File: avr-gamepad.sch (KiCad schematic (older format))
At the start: 31 parts, among them J1 Conn_01x08, P1 USB_C_Plug_USB2.0, SW1 RESET, SW10 Up, SW11 Down, SW12 Left, SW13 Select, SW2 R, SW3 X, SW4 A, SW5 B, SW6 Start, SW7 Y, SW8 Right, SW9 L, U1 ATmega32U4-AU, Y1 16 MHz

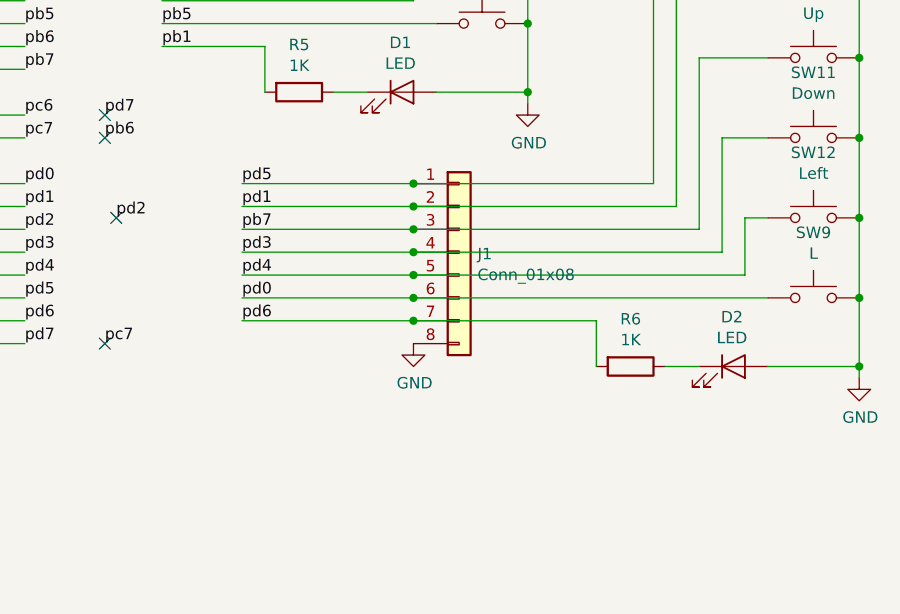
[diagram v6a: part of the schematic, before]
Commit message: kill the double sided feature, make it 2 boards, import mousebites
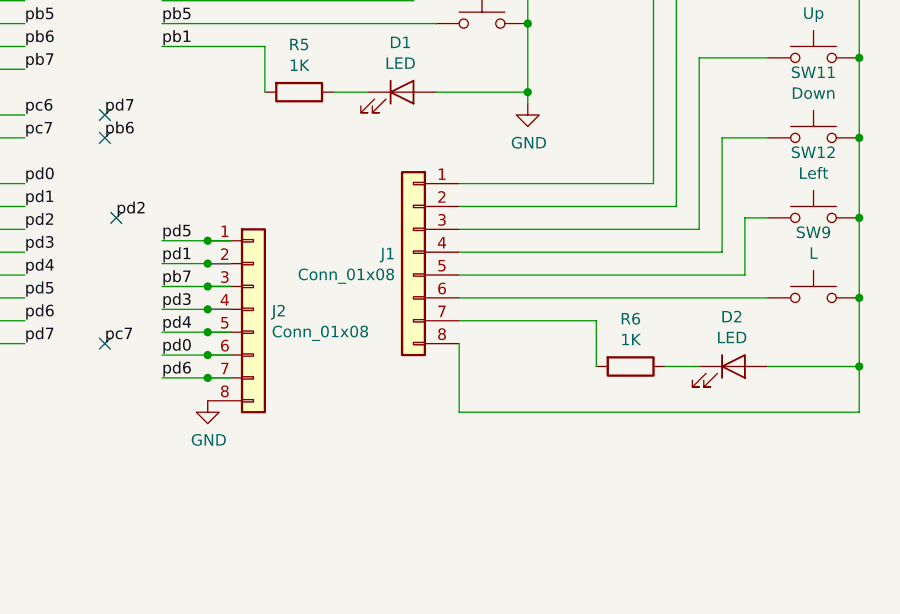
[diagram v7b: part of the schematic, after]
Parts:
- added J2: Conn_01x08, Connector_FFC-FPC:Hirose_FH12-8S-0.5SH_1x08-1MP_P0.50mm_Horizontal, symbol Connector_Generic:Conn_01x08
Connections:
- wire segments 135 -> 144
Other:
- moved on the sheet: J1
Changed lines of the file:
@@
 	6600 850  7100 850
 Connection ~ 8950 3800
-$Comp
-L power:GND #PWR0115
-U 1 1 5CF1335E
-P 8950 4150
-F 0 "#PWR0115" H 8950 3900 50  0001 C CNN
-F 1 "GND" H 8955 3977 50  0000 C CNN
-F 2 "" H 8950 4150 50  0001 C CNN
-F 3 "" H 8950 4150 50  0001 C CNN
-	1    8950 4150
-	1    0    0    -1
-$EndComp
 Wire Wire Line
 	8950 3450 8950 3800
@@
 	8550 4100 8950 4100
 Connection ~ 8950 4100
-Wire Wire Line
-	8950 4100 8950 4150
 Wire Wire Line
 	7800 4100 7800 3900
@@
 	1400 4400 1400 4550
 Wire Wire Line
-	6250 3900 7000 3900
-Wire Wire Line
-	6250 3800 7000 3800
-Wire Wire Line
-	6250 3700 7000 3700
-Wire Wire Line
-	6250 3600 7000 3600
-Wire Wire Line
-	6250 3500 7000 3500
-Wire Wire Line
-	6250 3400 7000 3400
-Wire Wire Line
-	6250 3300 7000 3300
-Connection ~ 7000 3300
-Wire Wire Line
-	7000 3300 8050 3300
-Connection ~ 7000 3400
-Wire Wire Line
-	7000 3400 8150 3400
-Connection ~ 7000 3500
-Wire Wire Line
-	7000 3500 8250 3500
-Connection ~ 7000 3600
-Wire Wire Line
-	7000 3600 8350 3600
-Connection ~ 7000 3700
-Wire Wire Line
-	7000 3700 8450 3700
-Connection ~ 7000 3800
-Wire Wire Line
-	7000 3800 8550 3800
-Connection ~ 7000 3900
-Wire Wire Line
-	7000 3900 7800 3900
+	5900 4150 6100 4150
+Wire Wire Line
+	5900 4050 6100 4050
+Wire Wire Line
+	5900 3950 6100 3950
+Wire Wire Line
+	5900 3850 6100 3850
+Wire Wire Line
+	5900 3750 6100 3750
+Wire Wire Line
+	5900 3650 6100 3650
+Wire Wire Line
+	5900 3550 6100 3550
 Text Label 5300 2800 0    50   ~ 0
 pb7
@@
 Text Label 5900 2600 0    50   ~ 0
 pb5
-Text Label 6250 3400 0    50   ~ 0
+Text Label 5900 3650 0    50   ~ 0
 pd1
 Text Label 5700 3450 0    50   ~ 0
 pd2
-Text Label 6250 3600 0    50   ~ 0
+Text Label 5900 3850 0    50   ~ 0
 pd3
-Text Label 6250 3700 0    50   ~ 0
+Text Label 5900 3950 0    50   ~ 0
 pd4
-Text Label 6250 3300 0    50   ~ 0
+Text Label 5900 3550 0    50   ~ 0
 pd5
 Text Label 5650 3000 0    50   ~ 0
@@
 	5100 3900 5300 3900
 NoConn ~ 5700 3450
-Text Label 6250 3500 0    50   ~ 0
+Text Label 5900 3750 0    50   ~ 0
 pb7
 NoConn ~ 5100 4300
@@
 	1    0    0    -1
 $EndComp
-Text Label 6250 3900 0    50   ~ 0
+Text Label 5900 4150 0    50   ~ 0
 pd6
 NoConn ~ 5650 3000
 NoConn ~ 5650 4000
-$Comp
-L power:GND #PWR0113
-U 1 1 5D261ED2
-P 7000 4000
-F 0 "#PWR0113" H 7000 3750 50  0001 C CNN
-F 1 "GND" H 7005 3827 50  0000 C CNN
-F 2 "" H 7000 4000 50  0001 C CNN
-F 3 "" H 7000 4000 50  0001 C CNN
-	1    7000 4000
-	1    0    0    -1
-$EndComp
-$Comp
-L Connector_Generic:Conn_01x08 J1
-U 1 1 5CF089CD
-P 7200 3600
-F 0 "J1" H 7280 3592 50  0000 L CNN
-F 1 "Conn_01x08" H 7280 3501 50  0000 L CNN
-F 2 "Connector_FFC-FPC:Hirose_FH12-8S-0.5SH_1x08-1MP_P0.50mm_Horizontal" H 7200 3600 50  0001 C CNN
-F 3 "~" H 7200 3600 50  0001 C CNN
-	1    7200 3600
-	1    0    0    -1
-$EndComp
 Text Label 5650 4000 0    50   ~ 0
 pc7
@@
 Text Label 5900 2100 0    50   ~ 0
 pb3
-Text Label 6250 3800 0    50   ~ 0
+Text Label 5900 4050 0    50   ~ 0
 pd0
 $Comp
@@
 Wire Wire Line
 	1150 1850 2350 1850
+$Comp
+L Connector_Generic:Conn_01x08 J2
+U 1 1 5D94373B
+P 6300 3850
+F 0 "J2" H 6380 3842 50  0000 L CNN
+F 1 "Conn_01x08" H 6380 3751 50  0000 L CNN
+F 2 "Connector_FFC-FPC:Hirose_FH12-8S-0.5SH_1x08-1MP_P0.50mm_Horizontal" H 6300 3850 50  0001 C CNN
+F 3 "~" H 6300 3850 50  0001 C CNN
+	1    6300 3850
+	1    0    0    -1
+$EndComp
+Connection ~ 6100 3550
+Wire Wire Line
+	6100 3550 6200 3550
+Connection ~ 6100 3650
+Wire Wire Line
+	6100 3650 6200 3650
+Connection ~ 6100 3750
+Wire Wire Line
+	6100 3750 6200 3750
+Connection ~ 6100 3850
+Wire Wire Line
+	6100 3850 6200 3850
+Connection ~ 6100 3950
+Wire Wire Line
+	6100 3950 6200 3950
+Connection ~ 6100 4050
+Wire Wire Line
+	6100 4050 6200 4050
+Connection ~ 6100 4150
+Wire Wire Line
+	6100 4150 6200 4150
+Wire Wire Line
+	7200 3900 7800 3900
+Wire Wire Line
+	7200 3800 8550 3800
+Wire Wire Line
+	7200 3700 8450 3700
+Wire Wire Line
+	7200 3600 8350 3600
+Wire Wire Line
+	7200 3500 8250 3500
+Wire Wire Line
+	7200 3400 8150 3400
+Wire Wire Line
+	7200 3300 8050 3300
+$Comp
+L Connector_Generic:Conn_01x08 J1
+U 1 1 5CF089CD
+P 7000 3600
+F 0 "J1" H 7080 3592 50  0000 L CNN
+F 1 "Conn_01x08" H 7080 3501 50  0000 L CNN
+F 2 "Connector_FFC-FPC:Hirose_FH12-8S-0.5SH_1x08-1MP_P0.50mm_Horizontal" H 7000 3600 50  0001 C CNN
+F 3 "~" H 7000 3600 50  0001 C CNN
+	1    7000 3600
+	-1   0    0    -1
+$EndComp
+$Comp
+L power:GND #PWR0113
+U 1 1 5D9668CC
+P 6100 4250
+F 0 "#PWR0113" H 6100 4000 50  0001 C CNN
+F 1 "GND" H 6105 4077 50  0000 C CNN
+F 2 "" H 6100 4250 50  0001 C CNN
+F 3 "" H 6100 4250 50  0001 C CNN
+	1    6100 4250
+	1    0    0    -1
+$EndComp
+Wire Wire Line
+	8950 4300 7200 4300
+Wire Wire Line
+	7200 4300 7200 4000
+Wire Wire Line
+	8950 4100 8950 4300
 $EndSCHEMATC
